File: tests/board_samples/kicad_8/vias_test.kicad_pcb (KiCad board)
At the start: 4 copper layers, 40 x 40 mm, 2 parts, among them J1 USB_C_Receptacle, M1 MountingHole_2.1mm

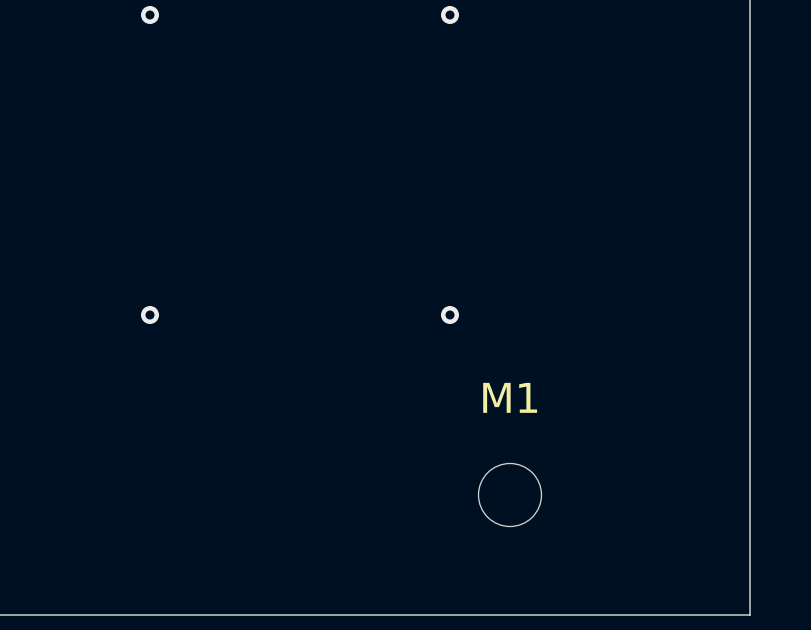
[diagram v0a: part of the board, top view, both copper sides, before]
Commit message: [Draw Fancy Stackup][Changed] Micro vias drawing
To look closer to real world, they only span 2 layers and they
must be stacked to span more layers.
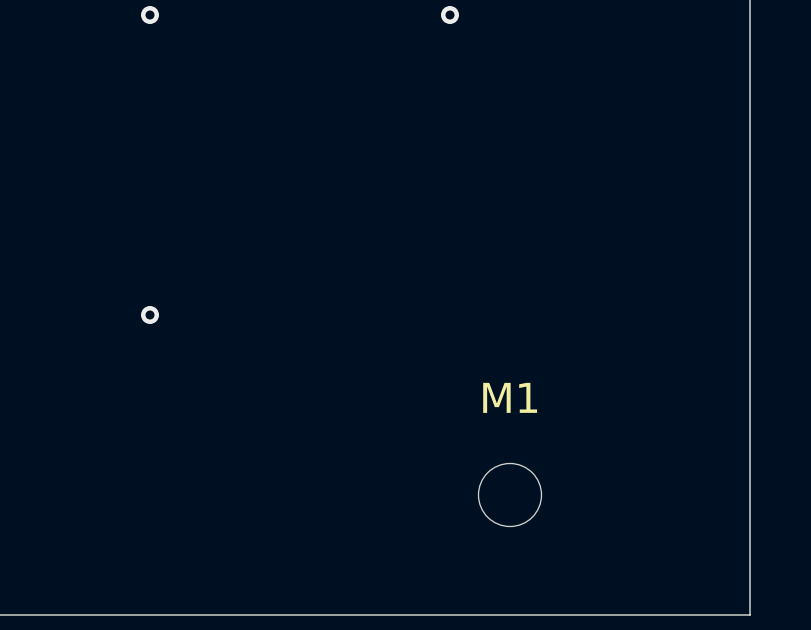
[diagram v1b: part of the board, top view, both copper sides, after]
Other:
- copper layers 4 -> 6
- board text added: "1.3mm"
- board text added: "Burried Via In1-In4"
- board text added: "In3.Cu"
- board text added: "In4.Cu"
- board text added: "Total thickness: 1.57mm"
- board text added: "Via F-In3"
- board text added: "Via In3-In4"
- board text removed: "0.1mm"
- board text removed: "1.24mm"
- board text removed: "Burried Via In1-In2"
- board text removed: "Total thickness: 1.6mm"
- board text removed: "Via F-In1"
- board text removed: "Via In2-B"
